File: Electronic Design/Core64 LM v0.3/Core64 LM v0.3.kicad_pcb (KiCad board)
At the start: 2 copper layers, 85 x 85 mm, 89 parts, among them J1 MOST CONNECTIONS PASS THROUGH, J2 MOST CONNECTIONS PASS THROUGH, J3 Conn_01x01_Male, J4 Conn_01x01_Male, J5 Conn_01x01_Male, J6 Conn_01x01_Male

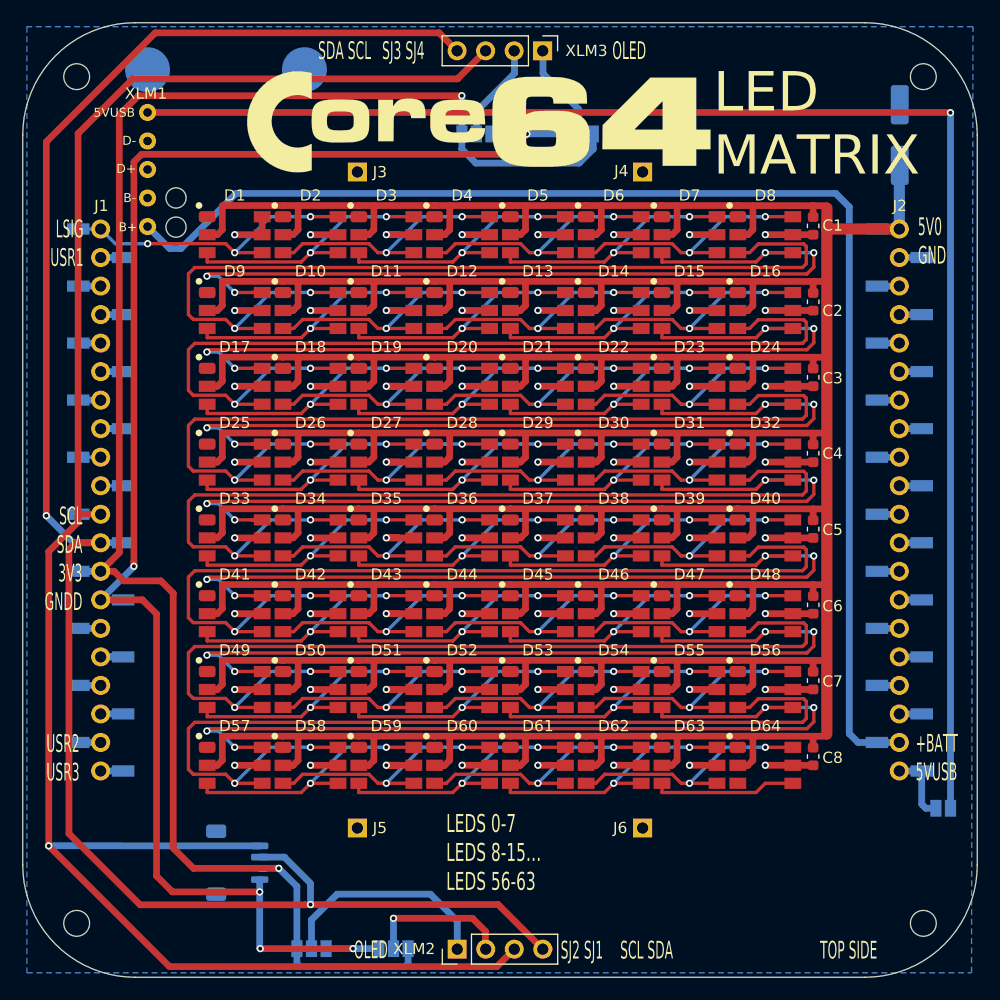
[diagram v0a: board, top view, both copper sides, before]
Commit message: Add opt. 5V0 buffer cap SMD and T.H., add PCB P/N, move corner holes to 37.7mm, move diffuser alignment mount points out and disconnect from GND, silkscreen cleanup
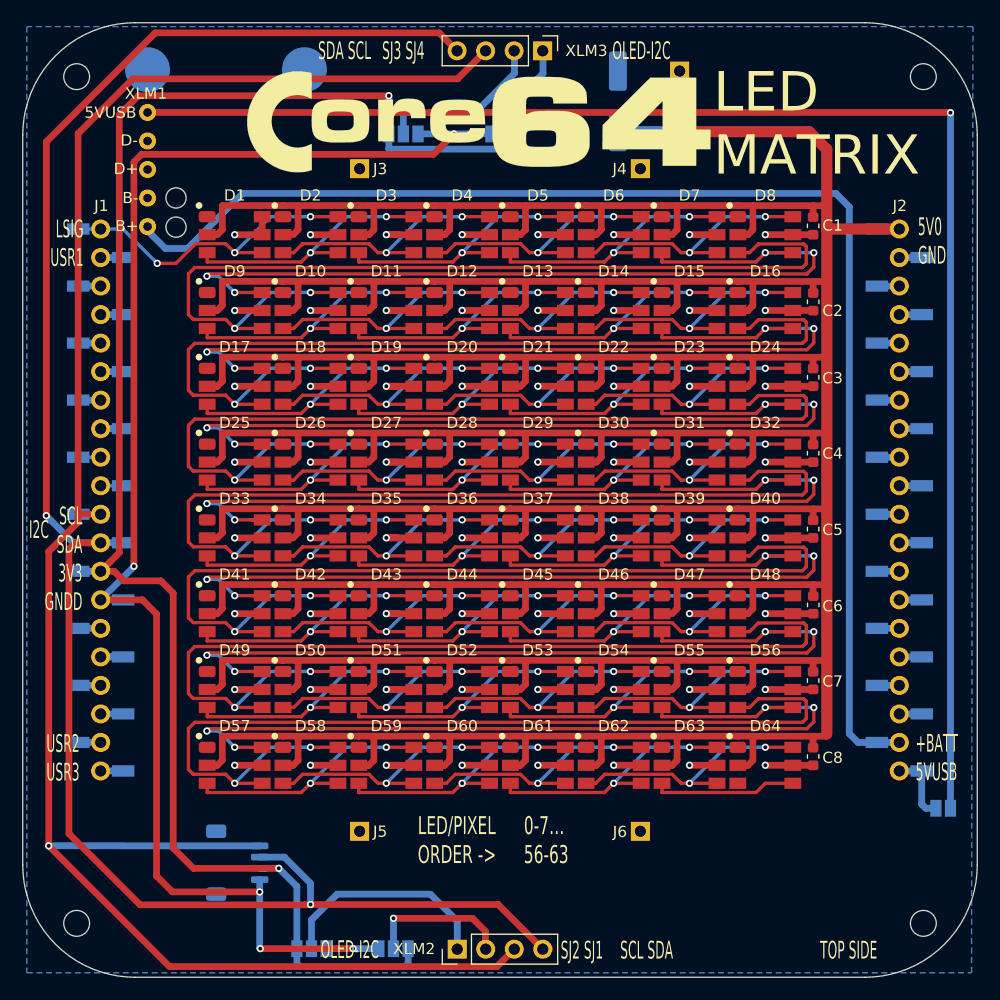
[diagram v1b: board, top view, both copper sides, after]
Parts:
- added J7: Conn_01x01_Male, Connector_PinHeader_2.54mm:PinHeader_1x01_P2.54mm_Vertical_No_Registration, B.Cu at (16.0, -32.8)
- added J8: Conn_01x01_Male, Connector_PinHeader_2.54mm:PinHeader_1x01_P2.54mm_Vertical_No_Registration, B.Cu at (16.0, -38.2)
- J1, J2: value MOST CONNECTIONS PASS THROUGH -> TSW-108-15-T-S
- moved C9 25.3 mm to (10.5, -35.5)
- moved JP3 6.50 mm to (-8.60, -32.6)
- moved JP4 6.50 mm to (0.50, -32.6)
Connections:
- J3 pad 1: GND -> Net-(J3-Pad1)
- J4 pad 1: GND -> Net-(J4-Pad1)
- J5 pad 1: GND -> Net-(J5-Pad1)
- J6 pad 1: GND -> Net-(J6-Pad1)
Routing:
- net 5V0: track 734.3 -> 752.9 mm
- net 3V3: track 155.6 -> 148.0 mm
- net GNDD: track 142.2 -> 135.7 mm
- net Net-(JP3-Pad2): track 8.80 -> 15.2 mm
- net LED_MATRIX_5V0_SIG: track 28.0 -> 29.5 mm
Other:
- board text added: "+"
- board text added: "0-7… 56-63"
- board text added: "<-Battery Corners"
- board text added: "BATTERY LIMITS: 1S OR 3.3-7.5V 3-4X “AA” or “AAA”"
- board text added: "CORE64 LED MATRIX (LM) Project information at www.Core64.io Designed by Andy Geppert at www.MachineIdeas.com PCB P/N: 132-001 V0.3 (2021-08-07) WS2813 LEDs"
- board text added: "GND"
- board text added: "I2C"
- board text added: "LED/PIXEL ORDER ->"
- board text added: "OLED-I2C"
- board text removed: "<-Battery Corner"
- board text removed: "Battery Limits: 1S or 3.3-7.5V"
- board text removed: "CORE64 LED MATRIX (LM) Project information at www.Core64.io Designed by Andy Geppert at www.MachineIdeas.com PCB P/N: 132-001 V0.3 (2021-05-21) WS2813 LEDs"
- board text removed: "LEDS 0-7 LEDS 8-15… LEDS 56-63"
- board text removed: "OLED"

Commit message: Core64 LED Matrix V0.3 release to manufacturing
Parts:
- D1, D10, D11, D12, D13, D14, D15, D16, D17, D18, D19, D2, D20, D21, D22, D23, D24, D25, D26, D27, D28, D29, D3, D30, D31, D32, D33, D34, D35, D36, D37, D38, D39, D4, D40, D41, D42, D43, D44, D45, D46, D47, D48, D49, D5, D50, D51, D52, D53, D54, D55, D56, D57, D58, D59, D6, D60, D61, D62, D63, D64, D7, D8, D9: value WS2813 -> WS2813C
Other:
- board text added: "<-4x “AA” Battery Corners"
- board text added: "<-LiPo Corners"
- board text added: "Add insulating layer between LiPo Charger and LM PCB"
- board text added: "CORE64 LED MATRIX (LM) Project information at www.Core64.io Designed by Andy Geppert | www.MachineIdeas.com PCB P/N: 132-001 V0.3 (2021-10-02) LEDS: WS2813C"
- board text removed: "<-Battery Corners"
- board text removed: "Add insulating layer between LiPo Charger and LM PCB."
- board text removed: "CORE64 LED MATRIX (LM) Project information at www.Core64.io Designed by Andy Geppert at www.MachineIdeas.com PCB P/N: 132-001 V0.3 (2021-08-07) WS2813 LEDs"
